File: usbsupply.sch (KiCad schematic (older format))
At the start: 11 parts

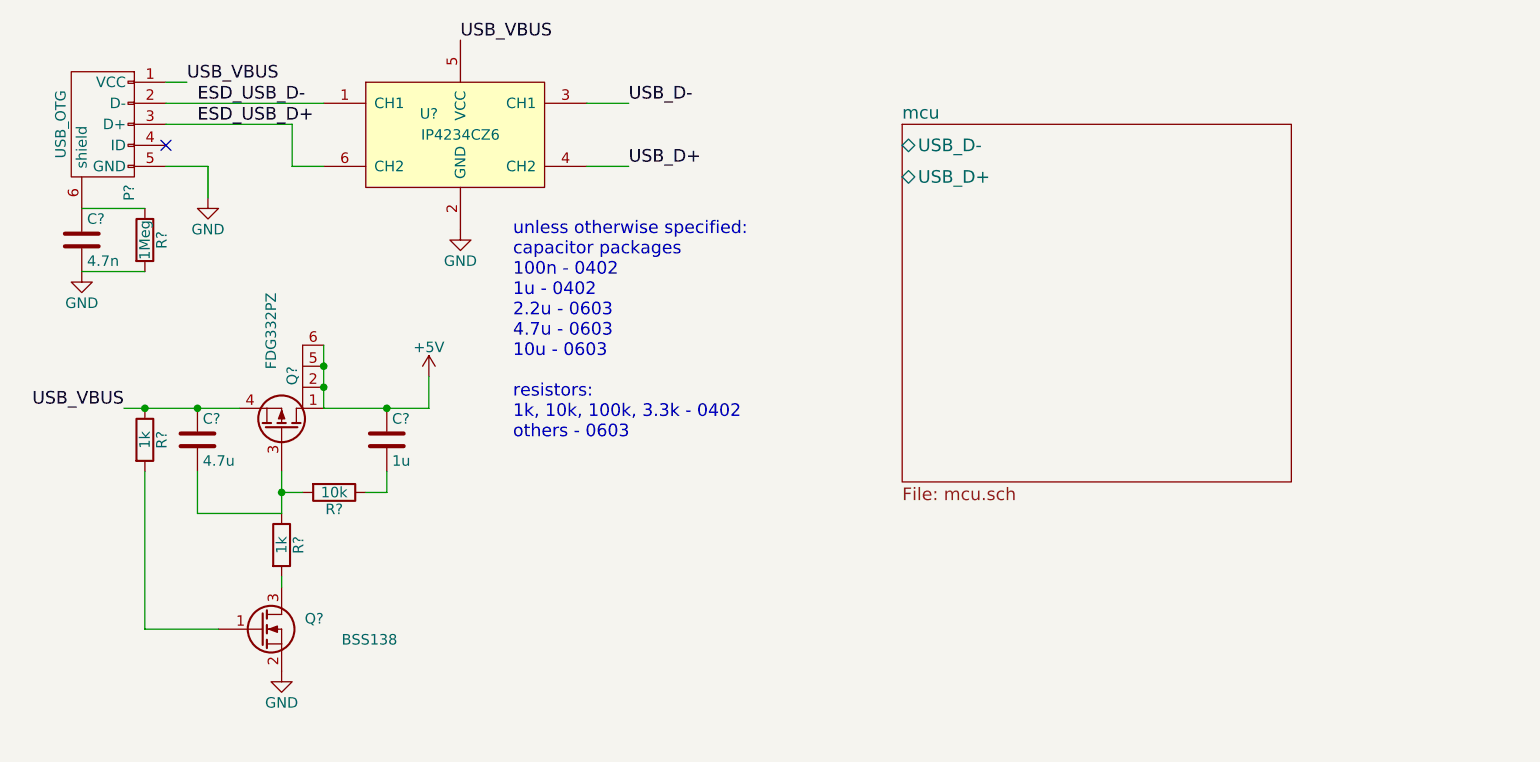
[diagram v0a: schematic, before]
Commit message: Finish basic MCU + USB/UART bridge schematics.
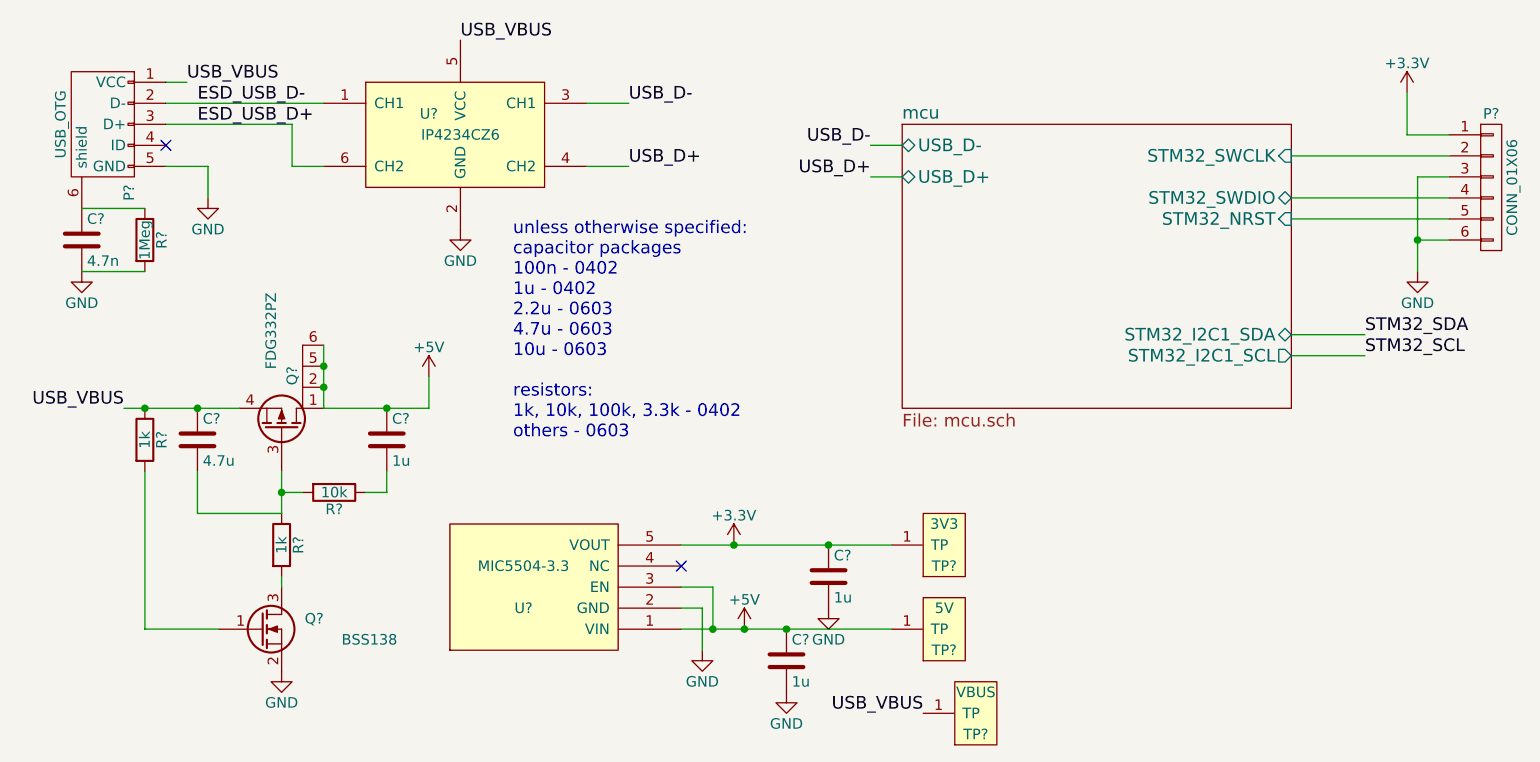
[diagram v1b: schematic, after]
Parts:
- added C? (x2): 1u, symbol C
- added P?: CONN_01X06, symbol CONN_01X06
- added TP?: 3V3, MODULE, symbol TP
- added TP?: 5V, MODULE, symbol TP
- added TP?: VBUS, MODULE, symbol TP
- added U?: MIC5504-3.3, MODULE, symbol MIC5504-3.3
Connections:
- net +5V: now also C?.1, TP?.1 (TP), U?.1 (VIN), U?.3 (EN)
- net GND: now also C?.2, C?.2, P?.3 (P3), P?.6 (P6), U?.2 (GND)
- net USB_VBUS: now also TP?.1 (TP)
- new net +3V3: C?.1, P?.1 (P1), TP?.1 (TP), U?.5 (VOUT)
- new net mcu/STM32_NRST: P?.5 (P5)
- new net mcu/STM32_SWCLK: P?.2 (P2)
- new net mcu/STM32_SWDIO: P?.4 (P4)
- no-connect marks 1 -> 2

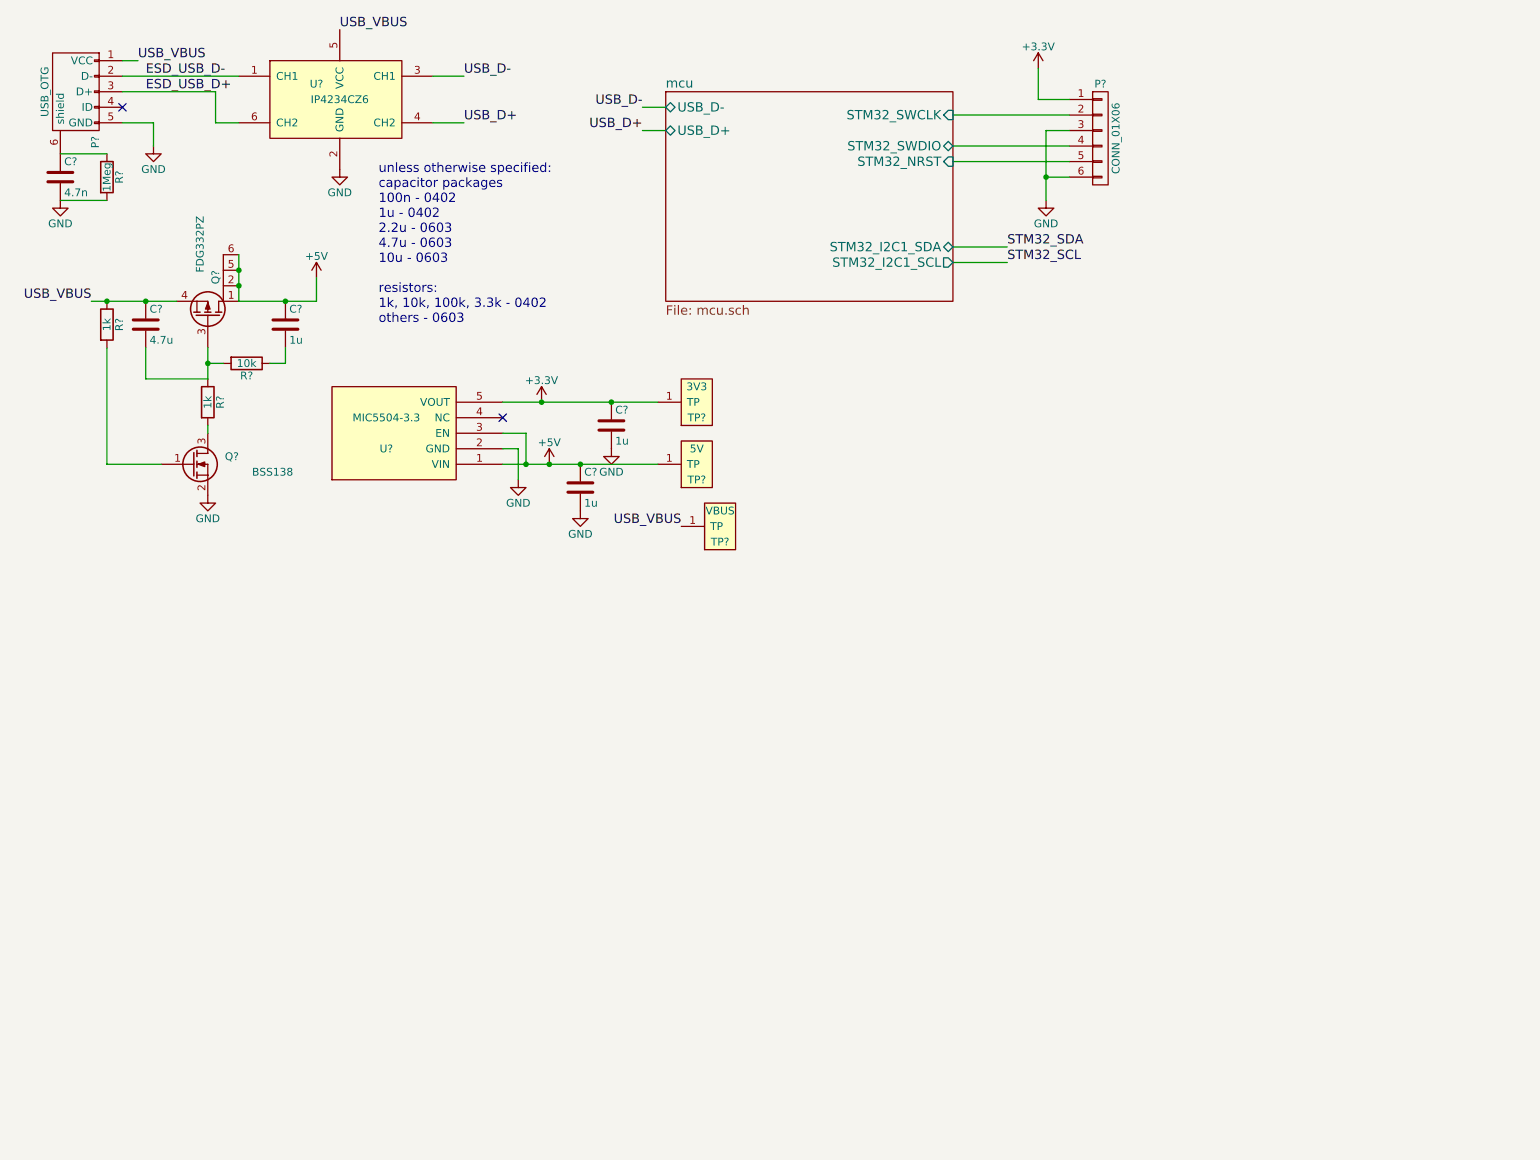
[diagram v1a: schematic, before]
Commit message: Completed most of the schematic work for the main LTC3883 IC.
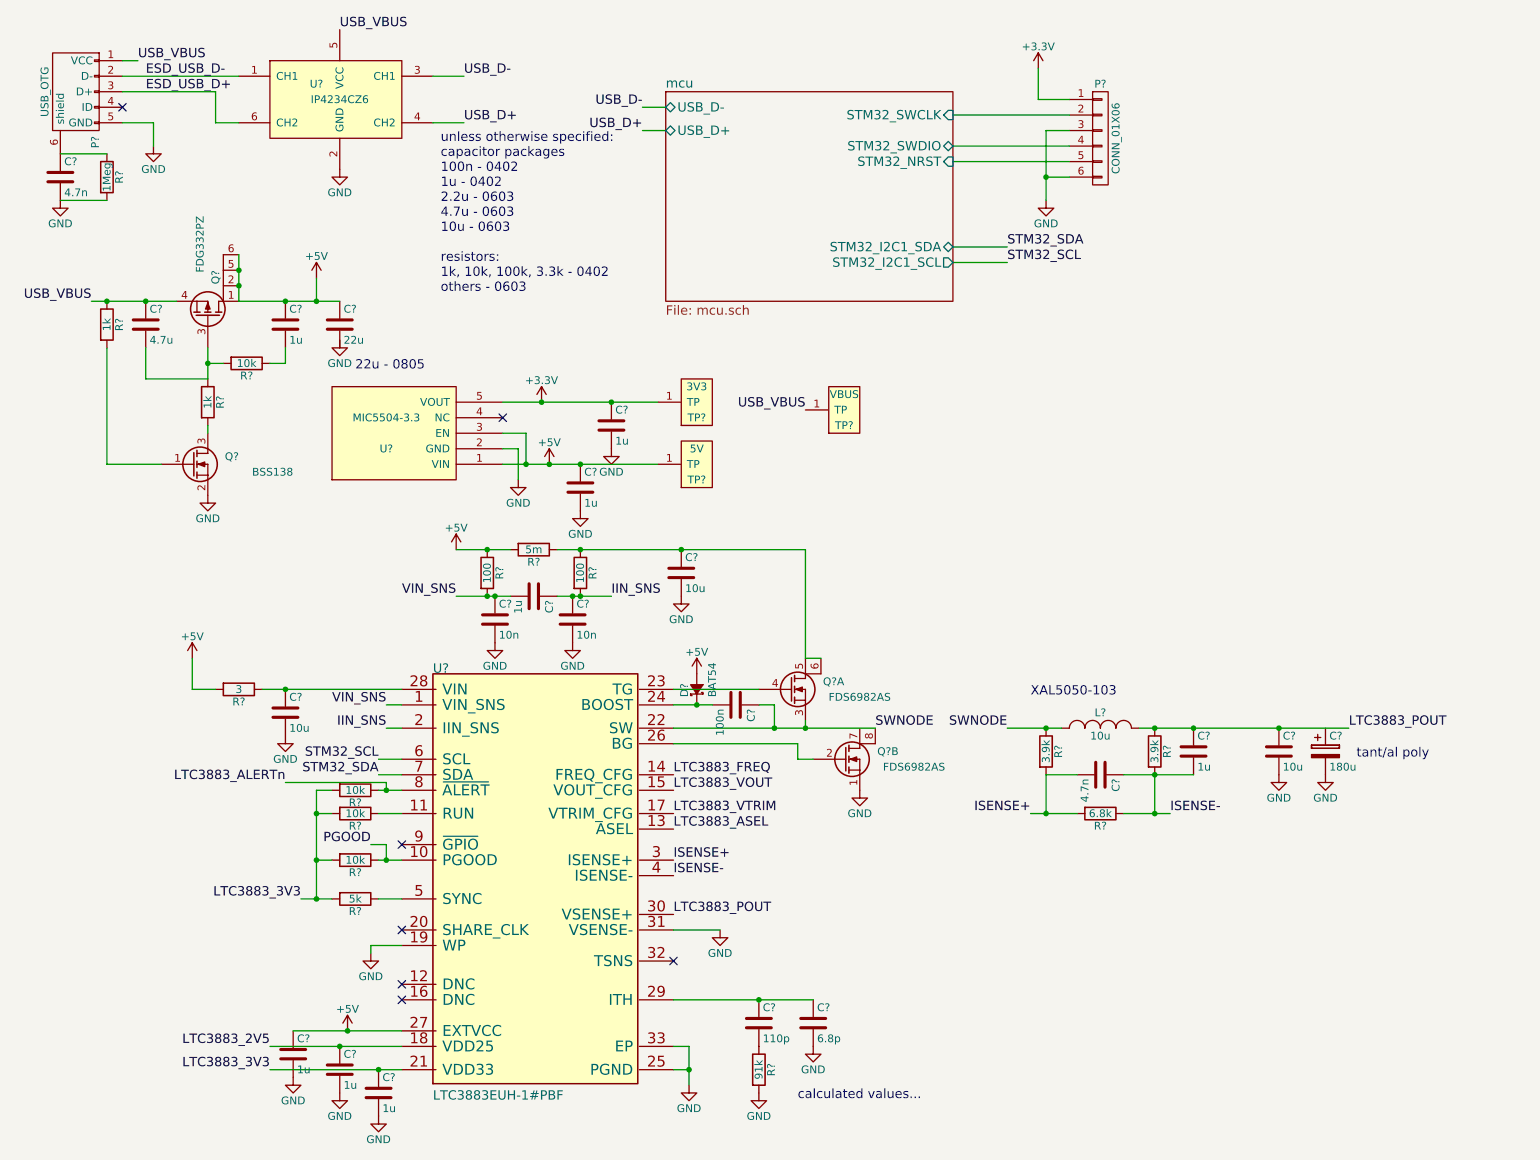
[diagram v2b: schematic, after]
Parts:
- added C?: 22u, symbol C
- added C? (x5): 1u, symbol C
- added C? (x3): 10u, symbol C
- added C? (x2): 10n, symbol C
- added C?: 100n, symbol C
- added C?: 4.7n, symbol C
- added C?: 110p, symbol C
- added C?: 6.8p, symbol C
- added C?: 180u, symbol CP
- added D?: BAT54, symbol D_Schottky_Small
- added L?: 10u, symbol INDUCTOR_SMALL
- added Q? (x2): FDS6982AS, symbol FDS6982AS
- added R?: 5k, symbol R
- added R? (x3): 10k, symbol R
- added R?: 3, symbol R
- added R?: 5m, symbol R
- added R? (x2): 100, symbol R
- added R? (x2): 3.9k, symbol R
- added R?: 6.8k, symbol R
- added R?: 91k, symbol R
- added U?: LTC3883EUH-1#PBF, symbol LTC3883EUH-1#PBF
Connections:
- net +5V: now also C?.1, C?.1, D?.2 (A), R?.1, R?.2, R?.2, U?.27 (EXTVCC)
- net GND: now also C?.2, C?.2, C?.2, C?.2, C?.2, C?.2, C?.2, C?.2, C?.2, C?.2, Q?.1 (S), R?.2, U?.19 (WP), U?.25 (PGND), U?.31 (VSENSE-), U?.33 (EP)
- net STM32_SCL: now also U?.6 (SCL)
- net STM32_SDA: now also U?.7 (SDA)
- new net: R?.1, U?.11 (RUN)
- new net: Q?.4 (G), U?.23 (TG)
- new net: C?.2, D?.1 (K), U?.24 (BOOST)
- new net: Q?.2 (G), U?.26 (BG)
- new net: C?.1, R?.1, U?.28 (VIN)
- new net: C?.1, C?.1, U?.29 (ITH)
- new net: R?.1, U?.5 (SYNC)
- new net: C?.1, Q?.5 (D), Q?.6 (D), R?.1, R?.1
- new net: C?.2, R?.1
- new net IIN_SNS: C?.1, C?.1, R?.2, U?.2 (IIN_SNS)
- new net ISENSE+: C?.2, R?.2, R?.2, U?.3 (ISENSE+)
- new net ISENSE-: C?.1, C?.2, R?.1, R?.2, U?.4 (ISENSE-)
- new net LTC3883_2V5: C?.1, U?.18 (VDD25)
- new net LTC3883_3V3: C?.1, R?.2, R?.2, R?.2, R?.2, U?.21 (VDD33)
- new net LTC3883_ALERTn: R?.1, U?.8 (~ALERT)
- new net LTC3883_ASEL: U?.13 (ASEL)
- new net LTC3883_FREQ: U?.14 (FREQ_CFG)
- new net LTC3883_POUT: C?.1, C?.1, L?.2, R?.1, U?.30 (VSENSE+)
- new net LTC3883_VOUT: U?.15 (VOUT_CFG)
- new net LTC3883_VTRIM: U?.17 (VTRIM_CFG)
- new net PGOOD: R?.1, U?.10 (PGOOD)
- new net SWNODE: C?.1, L?.1, Q?.3 (S), Q?.8 (D), R?.1, U?.22 (SW)
- new net VIN_SNS: C?.1, C?.2, R?.2, U?.1 (VIN_SNS)
- no-connect marks 2 -> 7
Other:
- note added: "22u - 0805"
- note added: "XAL5050-103"
- note added: "calculated values...\n"
- note added: "tant/al poly\n"
- moved on the sheet: TP?

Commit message: Add the config resistor dividers to the LTC3883 and output connectors, and a handful of test points. Schematic probably almost done at this point.
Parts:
- added P3: VOUT_CONN, symbol CONN_01X04
- added P4: GND_CONN, symbol CONN_01X04
- added R14: 20k, symbol R
- added R15: 12.7k, symbol R
- added R18, R21: 10k, symbol R
- added R19, R22: 15.8k, symbol R
- added TP4: SW, MODULE, symbol TP
- added TP5: TG, MODULE, symbol TP
- added TP6: BG, MODULE, symbol TP
- added TP7: 2V5, MODULE, symbol TP
- P2: renamed from P?; value CONN_01X06 -> SWD_CONN
- gave numbers to parts that had none: 49
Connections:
- net GND: now also C6.2, P4.1 (P1), P4.2 (P2), P4.3 (P3), P4.4 (P4), R15.2, R19.2, R22.2
- net LTC3883_2V5: now also R14.1, R18.1, R21.1, TP7.1 (TP)
- net LTC3883_ASEL: now also R21.2, R22.1
- net LTC3883_FREQ: now also R14.2, R15.1
- net LTC3883_POUT: now also C21.1, P3.1 (P1), P3.2 (P2), P3.3 (P3), P3.4 (P4)
- net LTC3883_VOUT: now also R18.2, R19.1
- net SWNODE: now also Q3.7 (D), TP4.1 (TP)
- net TG: now reaches Q3.4 (G), U3.23 (TG)
- net TG: now also TP5.1 (TP)
- net BG: now reaches Q3.2 (G), U3.26 (BG)
- net BG: now also TP6.1 (TP)
- net LTC3883_VTRIM: no longer names the net of U3.17 (VTRIM_CFG)
- no-connect marks 7 -> 8
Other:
- note added: "3.3V Vout"
- note added: "500kHz switching frequency"
- note added: "addr lsbs 1110"
- note added: "all above resistors 1% tolerance"
